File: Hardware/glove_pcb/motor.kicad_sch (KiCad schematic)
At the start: 24 parts, among them J2 Conn_01x02, J3 Conn_01x02, J4 Conn_01x02, U3 DRV8876PWPR, U4 DRV8876PWPR, U5 DRV8876PWPR

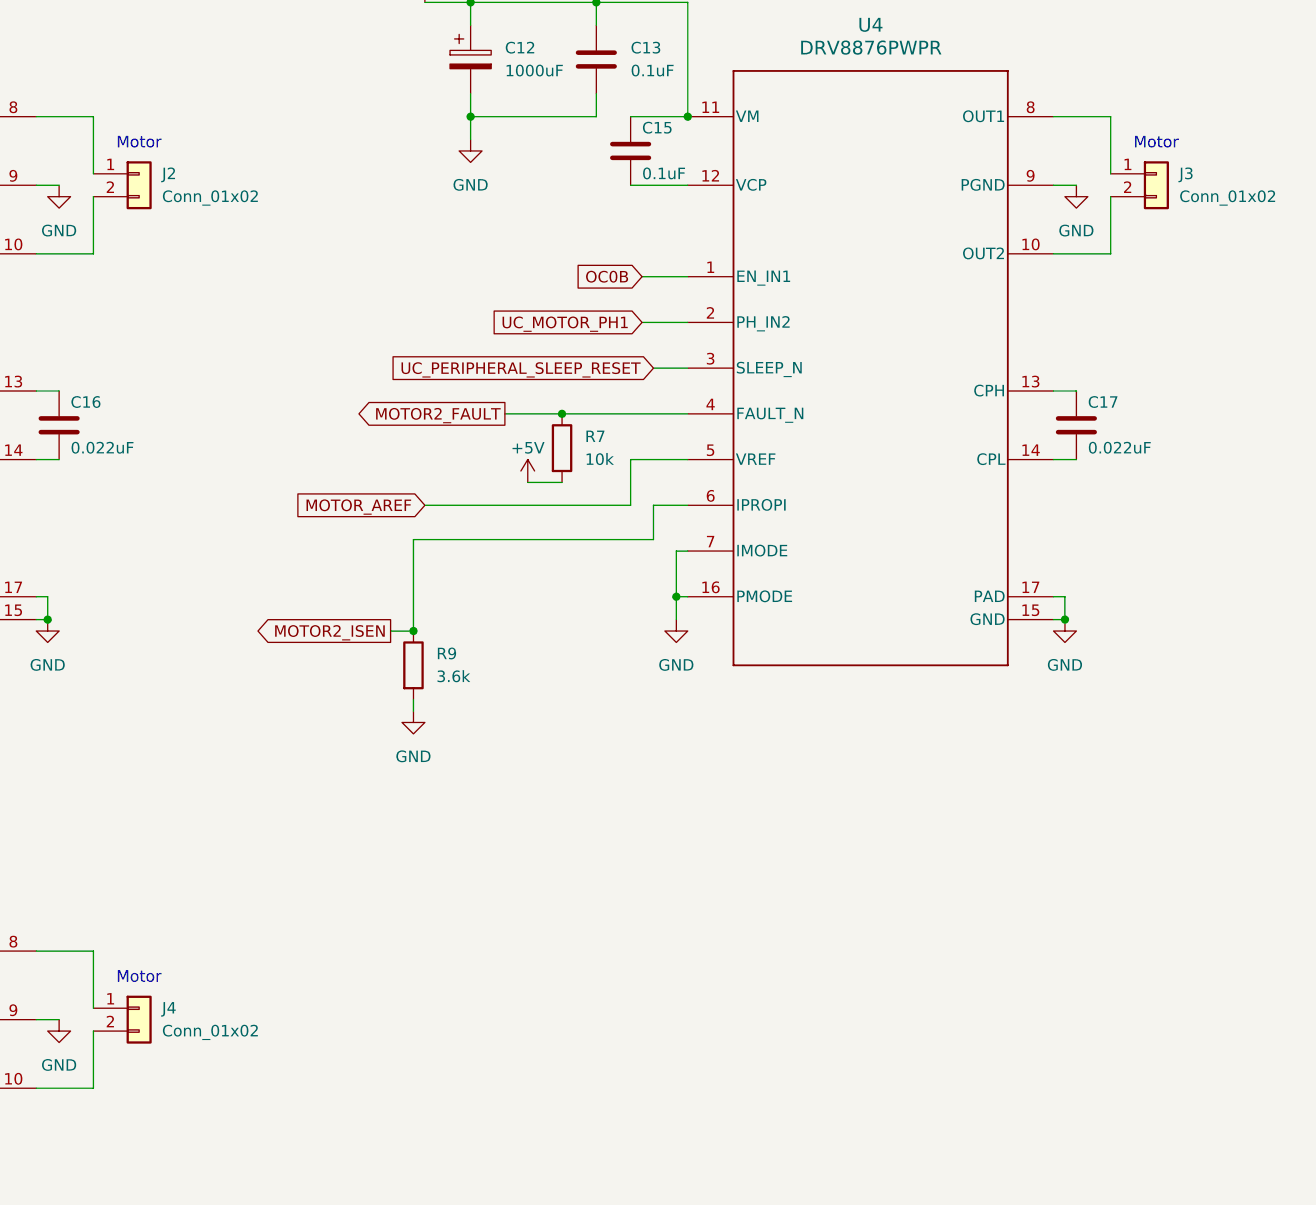
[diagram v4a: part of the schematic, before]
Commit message: More updates to the schematic based on Dmitry's feedback
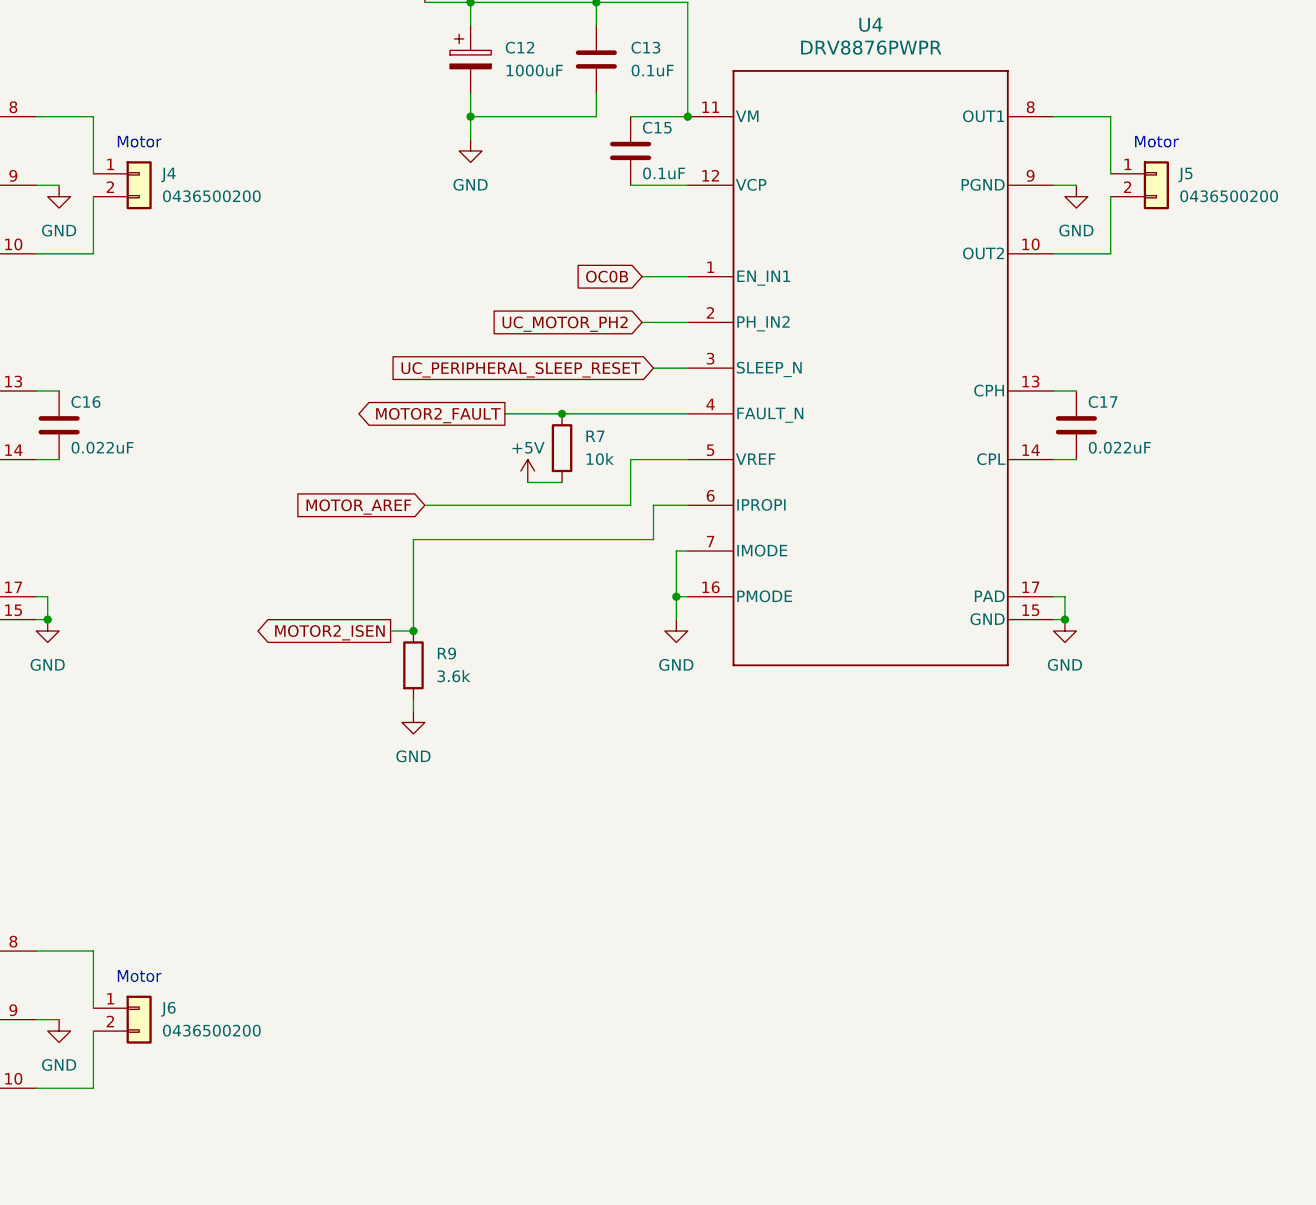
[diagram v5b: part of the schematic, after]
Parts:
- J4: renamed from J2; value Conn_01x02 -> 0436500200
- J5: renamed from J3; value Conn_01x02 -> 0436500200
- J6: renamed from J4; value Conn_01x02 -> 0436500200
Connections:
- net UC_MOTOR_PH1: no longer U4.2 (PH_IN2)
- net UC_MOTOR_PH2: now also U4.2 (PH_IN2)
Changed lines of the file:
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@@
   (title_block
     (title "Motor Drivers (1/2)")
-    (date "2023-11-24")
+    (date "2024-01-24")
     (company "COEN 490 Team 15")
   )
@@
     )
   )
-  (global_label "UC_MOTOR_PH1" (shape input) (at 190.5 57.15 180) (fields_autoplaced)
+  (global_label "UC_MOTOR_PH2" (shape input) (at 190.5 57.15 180) (fields_autoplaced)
     (effects (font (size 1.27 1.27)) (justify right))
     (property "Intersheetrefs" "${INTERSHEET_REFS}" (at 172.8191 57.15 0)
@@
   (symbol (lib_id "Connector_Generic:Conn_01x02") (at 134.62 133.35 0) (unit 1)
     (in_bom yes) (on_board yes) (dnp no) (fields_autoplaced)
-    (property "Reference" "J4" (at 137.16 133.35 0)
-      (effects (font (size 1.27 1.27)) (justify left))
-    )
-    (property "Value" "Conn_01x02" (at 137.16 135.89 0)
+    (property "Reference" "J6" (at 137.16 133.35 0)
+      (effects (font (size 1.27 1.27)) (justify left))
+    )
+    (property "Value" "0436500200" (at 137.16 135.89 0)
       (effects (font (size 1.27 1.27)) (justify left))
     )
@@
       (project "glove_pcb"
         (path "/747ff5f3-d342-40b0-8e4e-75b3a3063e75/c30ce3a0-a40a-4a3c-9b4e-a16a5a73dc39"
+          (reference "J6") (unit 1)
+        )
+      )
+    )
+  )
+  (symbol (lib_id "Connector_Generic:Conn_01x02") (at 134.62 40.64 0) (unit 1)
+    (in_bom yes) (on_board yes) (dnp no) (fields_autoplaced)
+    (property "Reference" "J4" (at 137.16 40.64 0)
+      (effects (font (size 1.27 1.27)) (justify left))
+    )
+    (property "Value" "0436500200" (at 137.16 43.18 0)
+      (effects (font (size 1.27 1.27)) (justify left))
+    )
+    (property "Footprint" "Connector_Molex:Molex_Micro-Fit_3.0_43650-0215_1x02_P3.00mm_Vertical" (at 134.62 40.64 0)
+      (effects (font (size 1.27 1.27)) hide)
+    )
+    (property "Datasheet" "~" (at 134.62 40.64 0)
+      (effects (font (size 1.27 1.27)) hide)
+    )
+    (pin "1")
+    (pin "2")
+    (instances
+      (project "glove_pcb"
+        (path "/747ff5f3-d342-40b0-8e4e-75b3a3063e75/c30ce3a0-a40a-4a3c-9b4e-a16a5a73dc39"
           (reference "J4") (unit 1)
-        )
-      )
-    )
-  )
-  (symbol (lib_id "Connector_Generic:Conn_01x02") (at 134.62 40.64 0) (unit 1)
-    (in_bom yes) (on_board yes) (dnp no) (fields_autoplaced)
-    (property "Reference" "J2" (at 137.16 40.64 0)
-      (effects (font (size 1.27 1.27)) (justify left))
-    )
-    (property "Value" "Conn_01x02" (at 137.16 43.18 0)
-      (effects (font (size 1.27 1.27)) (justify left))
-    )
-    (property "Footprint" "Connector_Molex:Molex_Micro-Fit_3.0_43650-0215_1x02_P3.00mm_Vertical" (at 134.62 40.64 0)
-      (effects (font (size 1.27 1.27)) hide)
-    )
-    (property "Datasheet" "~" (at 134.62 40.64 0)
-      (effects (font (size 1.27 1.27)) hide)
-    )
-    (pin "1")
-    (pin "2")
-    (instances
-      (project "glove_pcb"
-        (path "/747ff5f3-d342-40b0-8e4e-75b3a3063e75/c30ce3a0-a40a-4a3c-9b4e-a16a5a73dc39"
-          (reference "J2") (unit 1)
         )
       )
@@
   (symbol (lib_id "Connector_Generic:Conn_01x02") (at 247.65 40.64 0) (unit 1)
     (in_bom yes) (on_board yes) (dnp no) (fields_autoplaced)
-    (property "Reference" "J3" (at 250.19 40.64 0)
-      (effects (font (size 1.27 1.27)) (justify left))
-    )
-    (property "Value" "Conn_01x02" (at 250.19 43.18 0)
+    (property "Reference" "J5" (at 250.19 40.64 0)
+      (effects (font (size 1.27 1.27)) (justify left))
+    )
+    (property "Value" "0436500200" (at 250.19 43.18 0)
       (effects (font (size 1.27 1.27)) (justify left))
     )
@@
       (project "glove_pcb"
         (path "/747ff5f3-d342-40b0-8e4e-75b3a3063e75/c30ce3a0-a40a-4a3c-9b4e-a16a5a73dc39"
-          (reference "J3") (unit 1)
-        )
-      )
+          (reference "J5") (unit 1)
+        )
+      )

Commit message: Change isp pin symbol
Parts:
- U3, U4, U5: footprint PWP0016J_N -> Glove_Footprints:PWP0016J_N
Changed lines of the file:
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@@
       (effects (font (size 1.524 1.524)))
     )
-    (property "Footprint" "PWP0016J_N" (at 102.87 62.23 0)
+    (property "Footprint" "Glove_Footprints:PWP0016J_N" (at 102.87 62.23 0)
       (effects (font (size 1.27 1.27) italic) hide)
     )
@@
       (effects (font (size 1.524 1.524)))
     )
-    (property "Footprint" "PWP0016J_N" (at 215.9 62.23 0)
+    (property "Footprint" "Glove_Footprints:PWP0016J_N" (at 215.9 62.23 0)
       (effects (font (size 1.27 1.27) italic) hide)
     )
@@
       (effects (font (size 1.524 1.524)))
     )
-    (property "Footprint" "PWP0016J_N" (at 102.87 154.94 0)
+    (property "Footprint" "Glove_Footprints:PWP0016J_N" (at 102.87 154.94 0)
       (effects (font (size 1.27 1.27) italic) hide)
     )

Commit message: Assign footprints and import all parts into pcb editor
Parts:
- J4, J5, J6: footprint Connector_Molex:Molex_Micro-Fit_3.0_43650-0215_1x02_P3.00mm_Vertical -> Connector_Molex:Molex_Micro-Fit_3.0_43650-0200_1x02_P3.00mm_Horizontal
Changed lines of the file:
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@@
       (effects (font (size 1.27 1.27)) (justify left))
     )
-    (property "Footprint" "Connector_Molex:Molex_Micro-Fit_3.0_43650-0215_1x02_P3.00mm_Vertical" (at 134.62 133.35 0)
+    (property "Footprint" "Connector_Molex:Molex_Micro-Fit_3.0_43650-0200_1x02_P3.00mm_Horizontal" (at 134.62 133.35 0)
       (effects (font (size 1.27 1.27)) hide)
     )
@@
       (effects (font (size 1.27 1.27)) (justify left))
     )
-    (property "Footprint" "Connector_Molex:Molex_Micro-Fit_3.0_43650-0215_1x02_P3.00mm_Vertical" (at 134.62 40.64 0)
+    (property "Footprint" "Connector_Molex:Molex_Micro-Fit_3.0_43650-0200_1x02_P3.00mm_Horizontal" (at 134.62 40.64 0)
       (effects (font (size 1.27 1.27)) hide)
     )
@@
       (effects (font (size 1.27 1.27)) (justify left))
     )
-    (property "Footprint" "Connector_Molex:Molex_Micro-Fit_3.0_43650-0215_1x02_P3.00mm_Vertical" (at 247.65 40.64 0)
+    (property "Footprint" "Connector_Molex:Molex_Micro-Fit_3.0_43650-0200_1x02_P3.00mm_Horizontal" (at 247.65 40.64 0)
       (effects (font (size 1.27 1.27)) hide)
     )

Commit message: Re-placing with new outline
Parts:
- J4, J5, J6: footprint Connector_Molex:Molex_Micro-Fit_3.0_43650-0200_1x02_P3.00mm_Horizontal -> Connector_JST:JST_PH_S2B-PH-K_1x02_P2.00mm_Horizontal
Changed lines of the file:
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@@
       (effects (font (size 1.27 1.27)) (justify left))
     )
-    (property "Footprint" "Connector_Molex:Molex_Micro-Fit_3.0_43650-0200_1x02_P3.00mm_Horizontal" (at 134.62 133.35 0)
+    (property "Footprint" "Connector_JST:JST_PH_S2B-PH-K_1x02_P2.00mm_Horizontal" (at 134.62 133.35 0)
       (effects (font (size 1.27 1.27)) hide)
     )
@@
       (effects (font (size 1.27 1.27)) (justify left))
     )
-    (property "Footprint" "Connector_Molex:Molex_Micro-Fit_3.0_43650-0200_1x02_P3.00mm_Horizontal" (at 134.62 40.64 0)
+    (property "Footprint" "Connector_JST:JST_PH_S2B-PH-K_1x02_P2.00mm_Horizontal" (at 134.62 40.64 0)
       (effects (font (size 1.27 1.27)) hide)
     )
@@
       (effects (font (size 1.27 1.27)) (justify left))
     )
-    (property "Footprint" "Connector_Molex:Molex_Micro-Fit_3.0_43650-0200_1x02_P3.00mm_Horizontal" (at 247.65 40.64 0)
+    (property "Footprint" "Connector_JST:JST_PH_S2B-PH-K_1x02_P2.00mm_Horizontal" (at 247.65 40.64 0)
       (effects (font (size 1.27 1.27)) hide)
     )
